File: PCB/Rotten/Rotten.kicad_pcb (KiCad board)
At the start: 2 copper layers, 56.5 x 61.6 mm, 43 parts, among them J1 Jack-DC, J2 FOOTSWITCH, J3 JACK OUTPUT, J4 JACK INPUT, Q1 2N5458, U1 AS301/OP07

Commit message: changed clipping diodes to 1N4148. Updated schematic and PCB images. Generated an HTML BOM.
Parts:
- D2, D3: value 1N4002 -> 1N4148
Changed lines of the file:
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@@
 		(tags "CP Radial series Radial pin pitch 2.00mm  diameter 5mm Electrolytic Capacitor")
 		(property "Reference" "C10"
-			(at 1 -3.75 360)
+			(at 1 -3.75 0)
 			(layer "F.SilkS")
 			(effects
@@
 		)
 		(property "Value" "4.7µF"
-			(at 1 3.75 360)
+			(at 1 3.75 0)
 			(layer "F.SilkS")
 			(effects
@@
 		)
 		(fp_text user "${REFERENCE}"
-			(at 1 0 360)
+			(at 1 0 0)
 			(layer "F.Fab")
 			(effects
@@
 		(tags "Resistor Axial_DIN0207 series Axial Horizontal pin pitch 7.62mm 0.25W = 1/4W length 6.3mm diameter 2.5mm")
 		(property "Reference" "R2"
-			(at 3.81 2.54 360)
+			(at 3.81 2.54 0)
 			(layer "F.SilkS")
 			(effects
@@
 		)
 		(property "Value" "100k"
-			(at 3.81 0 360)
+			(at 3.81 0 0)
 			(layer "F.SilkS")
 			(effects
@@
 		)
 		(fp_text user "${REFERENCE}"
-			(at 3.81 0 360)
+			(at 3.81 0 0)
 			(layer "F.Fab")
 			(effects
@@
 			)
 		)
-		(property "Value" "1N4002"
+		(property "Value" "1N4148"
 			(at 5.08 0 90)
 			(layer "F.SilkS")
@@
 		(tags "C Disc series Radial pin pitch 5.00mm  diameter 4.3mm width 1.9mm Capacitor")
 		(property "Reference" "C6"
-			(at -2.62 0 360)
+			(at -2.62 0 0)
 			(layer "F.SilkS")
 			(effects
@@
 		)
 		(property "Value" "100pF"
-			(at 2.5 0 360)
+			(at 2.5 0 0)
 			(layer "F.SilkS")
 			(effects
@@
 		)
 		(fp_text user "${REFERENCE}"
-			(at 2.5 0 360)
+			(at 2.5 0 0)
 			(layer "F.Fab")
 			(effects
@@
 		(tags "Resistor Axial_DIN0207 series Axial Horizontal pin pitch 7.62mm 0.25W = 1/4W length 6.3mm diameter 2.5mm")
 		(property "Reference" "R11"
-			(at 3.81 2.413 360)
+			(at 3.81 2.413 0)
 			(layer "F.SilkS")
 			(effects
@@
 		)
 		(property "Value" "1M"
-			(at 3.81 0 360)
+			(at 3.81 0 0)
 			(layer "F.SilkS")
 			(effects
@@
 		)
 		(fp_text user "${REFERENCE}"
-			(at 3.81 0 360)
+			(at 3.81 0 0)
 			(layer "F.Fab")
 			(effects
@@
 		(tags "C Disc series Radial pin pitch 5.00mm  diameter 4.3mm width 1.9mm Capacitor")
 		(property "Reference" "C7"
-			(at -2.58 0 360)
+			(at -2.58 0 0)
 			(layer "F.SilkS")
 			(effects
@@
 		)
 		(property "Value" "30pF"
-			(at 2.5 0 360)
+			(at 2.5 0 0)
 			(layer "F.SilkS")
 			(effects
@@
 		)
 		(fp_text user "${REFERENCE}"
-			(at 2.5 0 360)
+			(at 2.5 0 0)
 			(layer "F.Fab")
 			(effects
@@
 		)
 		(property "Value" "100k-A"
-			(at 2.54 2.54 360)
+			(at 2.54 2.54 0)
 			(layer "F.SilkS")
 			(effects
@@
 		)
 		(fp_text user "${REFERENCE}"
-			(at 0 2.54 360)
+			(at 0 2.54 0)
 			(layer "F.Fab")
 			(effects
@@
 		(tags "C Disc series Radial pin pitch 5.00mm  diameter 4.3mm width 1.9mm Capacitor")
 		(property "Reference" "C11"
-			(at 2.5 -2.2 360)
+			(at 2.5 -2.2 0)
 			(layer "F.SilkS")
 			(effects
@@
 		)
 		(property "Value" "3.3nF"
-			(at 2.5 0 360)
+			(at 2.5 0 0)
 			(layer "F.SilkS")
 			(effects
@@
 		)
 		(fp_text user "${REFERENCE}"
-			(at 2.5 0 360)
+			(at 2.5 0 0)
 			(layer "F.Fab")
 			(effects
@@
 		(tags "LED diameter 5.0mm 2 pins")
 		(property "Reference" "D4"
-			(at 1.27 -3.96 360)
+			(at 1.27 -3.96 0)
 			(layer "F.SilkS")
 			(effects
@@
 		)
 		(fp_text user "${REFERENCE}"
-			(at 1.25 0 360)
+			(at 1.25 0 0)
 			(layer "F.Fab")
 			(effects
@@
 		(tags "Through hole pin header THT 1x02 2.54mm single row")
 		(property "Reference" "J3"
-			(at 0 -2.33 360)
+			(at 0 -2.33 0)
 			(layer "F.SilkS")
 			(effects
@@
 		)
 		(property "Value" "JACK OUTPUT"
-			(at 0 4.87 360)
+			(at 0 4.87 0)
 			(layer "F.Fab")
 			(effects
@@
 		)
 		(property "Value" "Jack-DC"
-			(at 2.413 1.27 360)
+			(at 2.413 1.27 0)
 			(layer "F.SilkS")
 			(effects
@@
 		)
 		(fp_text user "${REFERENCE}"
-			(at 0 1.27 360)
+			(at 0 1.27 0)
 			(layer "F.Fab")
 			(effects
@@
 		)
 		(property "Value" "FOOTSWITCH"
-			(at -2.54 6.35 360)
+			(at -2.54 6.35 0)
 			(layer "F.SilkS")
 			(effects
@@
 		)
 		(fp_text user "${REFERENCE}"
-			(at 0 6.35 360)
+			(at 0 6.35 0)
 			(layer "F.Fab")
 			(effects
@@
 		)
 		(property "Value" "100k-A"
-			(at 2.54 2.54 360)
+			(at 2.54 2.54 0)
 			(layer "F.SilkS")
 			(effects
@@
 		)
 		(fp_text user "${REFERENCE}"
-			(at 0 2.54 360)
+			(at 0 2.54 0)
 			(layer "F.Fab")
 			(effects
@@
 		(tags "CP Radial series Radial pin pitch 2.00mm  diameter 5mm Electrolytic Capacitor")
 		(property "Reference" "C3"
-			(at 1 -3.75 360)
+			(at 1 -3.75 0)
 			(layer "F.SilkS")
 			(effects
@@
 		)
 		(property "Value" "1µF"
-			(at 1 3.75 360)
+			(at 1 3.75 0)
 			(layer "F.SilkS")
 			(effects
@@
 		)
 		(fp_text user "${REFERENCE}"
-			(at 1 0 360)
+			(at 1 0 0)
 			(layer "F.Fab")
 			(effects
@@
 		(tags "Resistor Axial_DIN0207 series Axial Horizontal pin pitch 7.62mm 0.25W = 1/4W length 6.3mm diameter 2.5mm")
 		(property "Reference" "R10"
-			(at 3.81 -2.37 360)
+			(at 3.81 -2.37 0)
 			(layer "F.SilkS")
 			(effects
@@
 		)
 		(property "Value" "1k5"
-			(at 3.81 0 360)
+			(at 3.81 0 0)
 			(layer "F.SilkS")
 			(effects
@@
 		)
 		(fp_text user "${REFERENCE}"
-			(at 3.81 0 360)
+			(at 3.81 0 0)
 			(layer "F.Fab")
 			(effects
@@
 			)
 		)
-		(property "Value" "1N4002"
+		(property "Value" "1N4148"
 			(at 5.08 0 90)
 			(layer "F.SilkS")
@@
 		(tags "C Disc series Radial pin pitch 5.00mm  diameter 4.3mm width 1.9mm Capacitor")
 		(property "Reference" "C12"
-			(at 2.46 2.159 360)
+			(at 2.46 2.159 0)
 			(layer "F.SilkS")
 			(effects
@@
 		)
 		(property "Value" "22nF"
-			(at 2.5 0 360)
+			(at 2.5 0 0)
 			(layer "F.SilkS")
 			(effects
@@
 		)
 		(fp_text user "${REFERENCE}"
-			(at 2.5 0 360)
+			(at 2.5 0 0)
 			(layer "F.Fab")
 			(effects
@@
 		)
 		(fp_text user "${REFERENCE}"
-			(at 0 2.54 360)
+			(at 0 2.54 0)
 			(layer "F.Fab")
 			(effects
@@
 	)
 	(zone
+		(net 18)
+		(net_name "Net-(D2-K)")
+		(layer "F.Cu")
+		(name "$teardrop_padvia$")
+		(hatch full 0.1)
+		(priority 30000)
+		(attr
+			(teardrop
+				(type padvia)
+			)
+		)
+		(connect_pads yes
+			(clearance 0)
+		)
+		(min_thickness 0.0254)
+		(filled_areas_thickness no)
+		(fill yes
+			(thermal_gap 0.5)
+			(thermal_bridge_width 0.5)
+			(island_removal_mode 1)
+			(island_area_min 10)
+		)
+		(polygon
+			(pts
+				(xy 138.14 65.967) (xy 138.14 66.367) (xy 139.794703 67.167) (xy 140.241 66.167) (xy 139.794703 65.167)
+			)
+		)
+	)
+	(zone
 		(net 6)
 		(net_name "Net-(C10-Pad1)")
@@
 		(name "$teardrop_padvia$")
 		(hatch full 0.1)
-		(priority 30003)
-		(attr
-			(teardrop
-				(type padvia)
-			)
-		)
-		(connect_pads yes
-			(clearance 0)
-		)
-		(min_thickness 0.0254)
-		(filled_areas_thickness no)
-		(fill yes
-			(thermal_gap 0.5)
-			(thermal_bridge_width 0.5)
-			(island_removal_mode 1)
-			(island_area_min 10)
-		)
-		(polygon
-			(pts
-				(xy 134.33 65.967) (xy 134.33 66.367) (xy 135.33 67.167) (xy 136.431 66.167) (xy 135.33 65.167)
-			)
-		)
-	)
-	(zone
-		(net 18)
-		(net_name "Net-(D2-K)")
-		(layer "F.Cu")
-		(name "$teardrop_padvia$")
-		(hatch full 0.1)
 		(priority 30010)
 		(attr
@@
 	)
 	(zone
+		(net 18)
+		(net_name "Net-(D2-K)")
+		(layer "F.Cu")
+		(name "$teardrop_padvia$")
+		(hatch full 0.1)
+		(priority 30002)
+		(attr
+			(teardrop
+				(type padvia)
+			)
+		)
+		(connect_pads yes
+			(clearance 0)
+		)
+		(min_thickness 0.0254)
+		(filled_areas_thickness no)
+		(fill yes
+			(thermal_gap 0.5)
+			(thermal_bridge_width 0.5)
+			(island_removal_mode 1)
+			(island_area_min 10)
+		)
+		(polygon
+			(pts
+				(xy 138.53 66.367) (xy 138.53 65.967) (xy 137.53 65.167) (xy 136.429 66.167) (xy 137.53 67.167)
+			)
+		)
+	)
+	(zone
 		(net 21)
 		(net_name "/VOUT")
@@
 	)
 	(zone
-		(net 18)
-		(net_name "Net-(D2-K)")
-		(layer "F.Cu")
-		(name "$teardrop_padvia$")
-		(hatch full 0.1)
-		(priority 30001)
-		(attr
-			(teardrop
-				(type padvia)
-			)
-		)
-		(connect_pads yes
-			(clearance 0)
-		)
-		(min_thickness 0.0254)
-		(filled_areas_thickness no)
-		(fill yes
-			(thermal_gap 0.5)
-			(thermal_bridge_width 0.5)
-			(island_removal_mode 1)
-			(island_area_min 10)
-		)
-		(polygon
-			(pts
-				(xy 138.14 65.967) (xy 138.14 66.367) (xy 139.794703 67.167) (xy 140.241 66.167) (xy 139.794703 65.167)
-			)
-		)
-	)
-	(zone
 		(net 6)
 		(net_name "Net-(C10-Pad1)")
@@
 		(name "$teardrop_padvia$")
 		(hatch full 0.1)
-		(priority 30002)
+		(priority 30001)
 		(attr
 			(teardrop
@@
 		(polygon
 			(pts
-				(xy 138.53 66.367) (xy 138.53 65.967) (xy 137.53 65.167) (xy 136.429 66.167) (xy 137.53 67.167)
+				(xy 134.33 65.967) (xy 134.33 66.367) (xy 135.33 67.167) (xy 136.431 66.167) (xy 135.33 65.167)
 			)
 		)

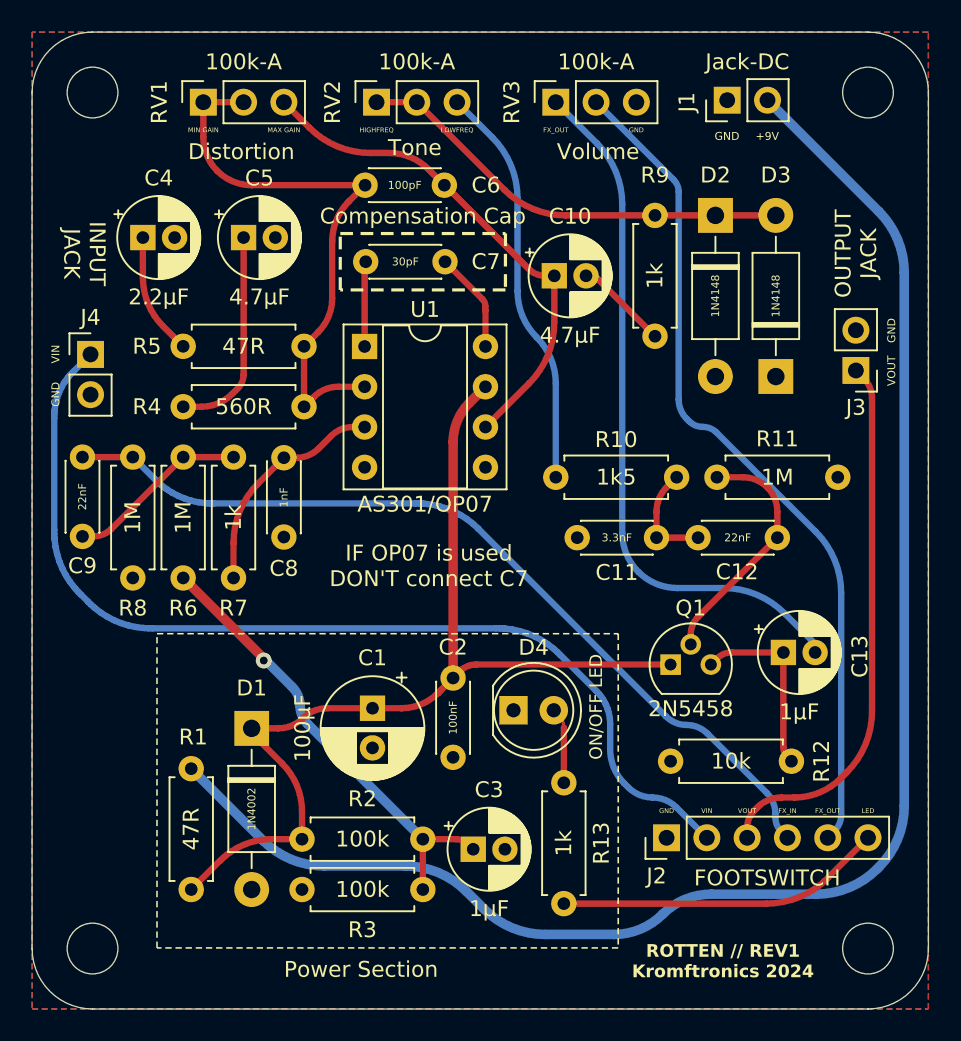
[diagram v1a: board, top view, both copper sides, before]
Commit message: Created Rev2 update! Fixed LED footswitch error that resulted in no light. Flipped "volume" and "gain" connections on PCB (1 -> 3). Fixed wrong pinout on JFET that resulted in no audio. Updated README with new images and better build descriptions.
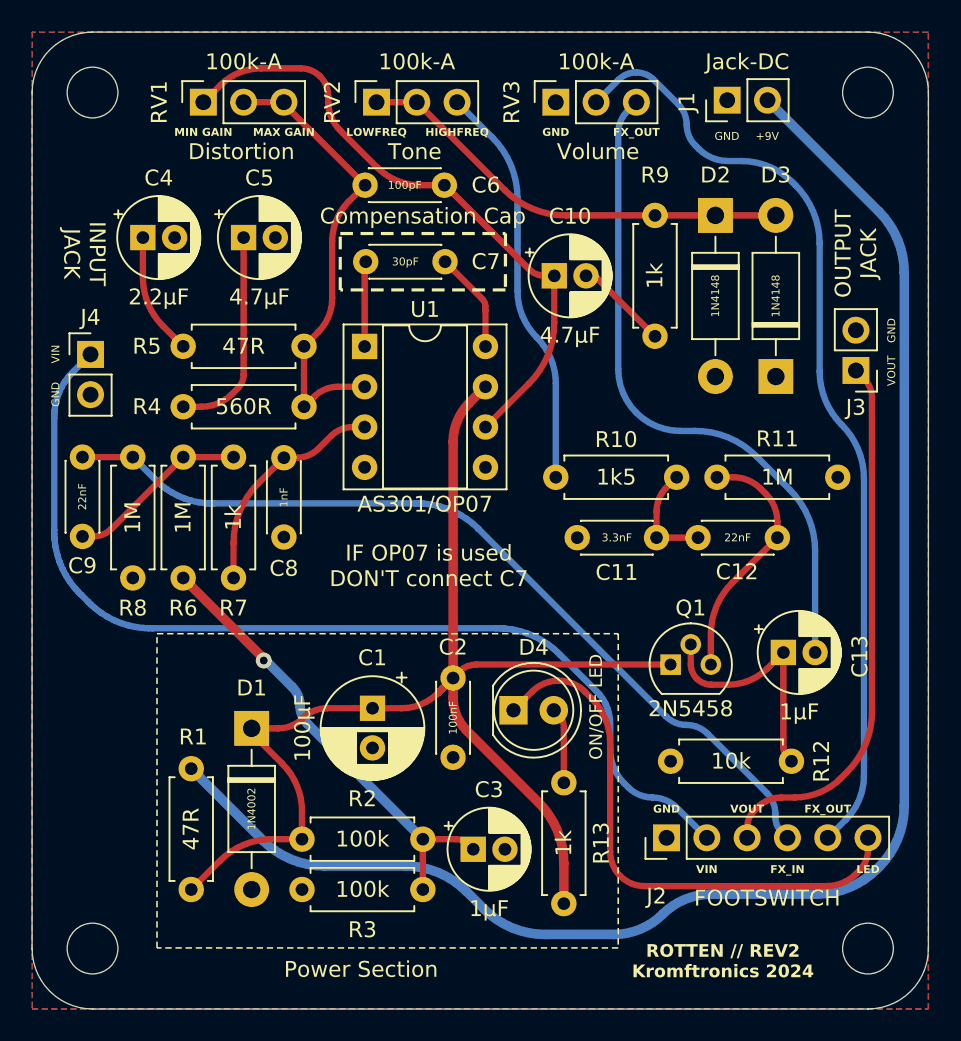
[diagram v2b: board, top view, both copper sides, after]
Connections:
- D4 pad 1: GND -> /LED
- Q1 pad 2: Net-(Q1-G) -> Net-(Q1-S)
- Q1 pad 3: Net-(Q1-S) -> Net-(Q1-G)
- R13 pad 2: /LED -> +9V
- RV1 pad 1: Net-(U1--) -> Net-(C10-Pad1)
- RV1 pad 3: Net-(C10-Pad1) -> Net-(U1--)
- RV3 pad 1: Net-(C13-Pad2) -> GND
- RV3 pad 3: GND -> Net-(C13-Pad2)
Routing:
- net +9V: track 62.8 -> 79.5 mm
- net /LED: track 20.6 -> 35.3 mm
- net Net-(C10-Pad1): track 31.9 -> 39.8 mm
- net Net-(U1--): track 35.6 -> 28.9 mm
- net /FX_OUT: track 53.1 -> 59.5 mm
- net Net-(Q1-S): track 11.9 -> 15.5 mm
- net Net-(C13-Pad2): track 44.4 -> 42.1 mm
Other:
- board text added: "ROTTEN // REV2 Kromftronics 2024"
- board text removed: "ROTTEN // REV1 Kromftronics 2024"

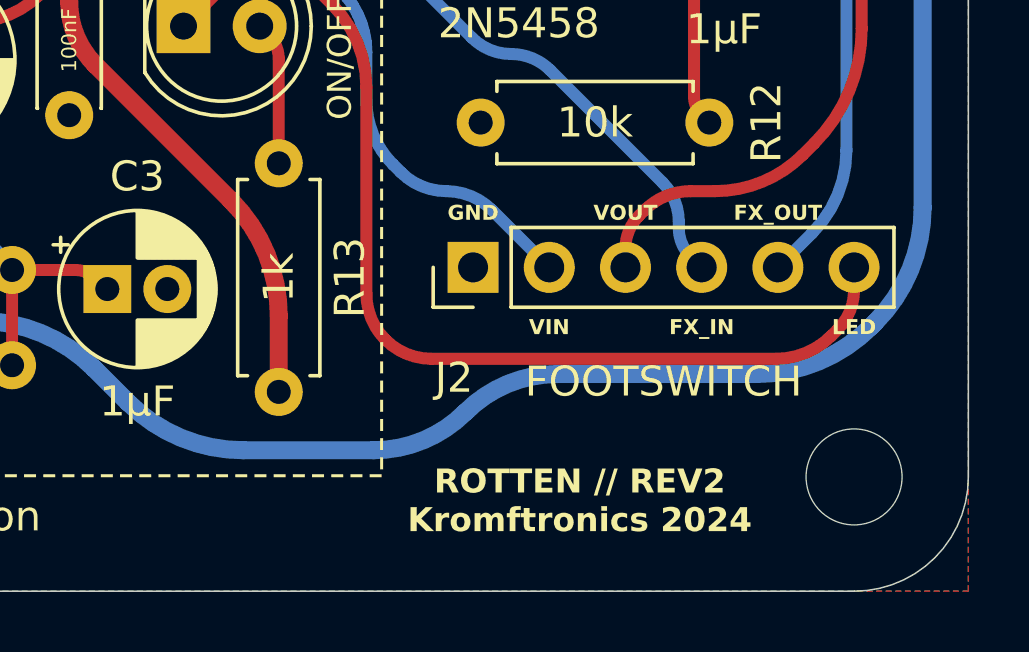
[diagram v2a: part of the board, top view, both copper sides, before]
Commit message: Added variable revision and issue date on the silkscreen, so I don't forget to update the rev and issue date on the silkscreen.
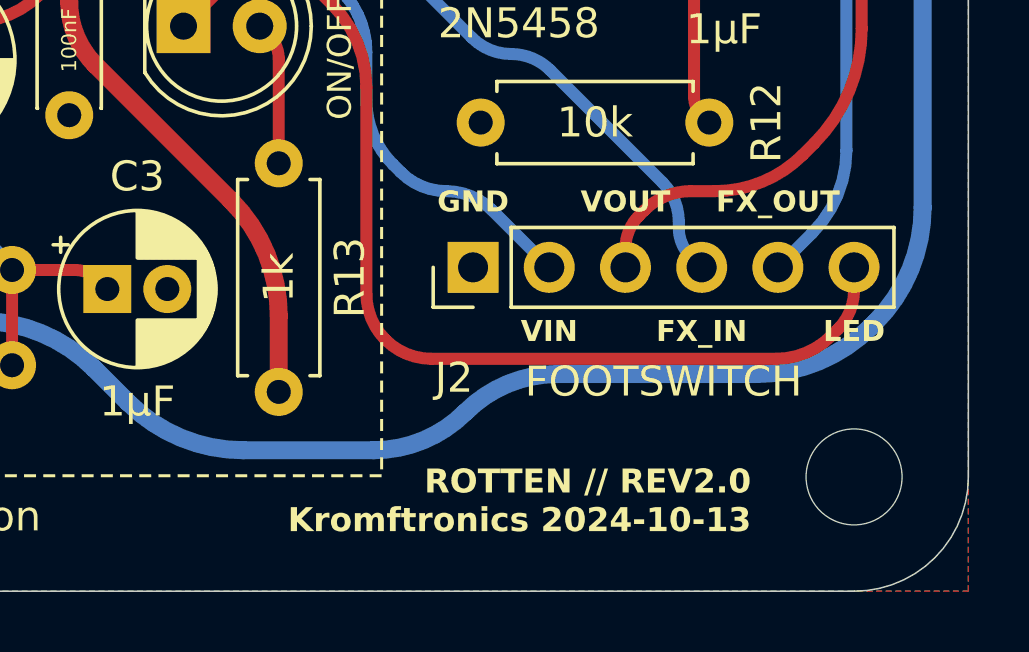
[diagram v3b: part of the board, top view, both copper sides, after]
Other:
- board text added: "ROTTEN // REV${REVISION} ${COMPANY} ${ISSUE_DATE}"
- board text removed: "ROTTEN // REV2 Kromftronics 2024"
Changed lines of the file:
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@@
 		(title "Rotten")
 		(date "2024-10-13")
-		(rev "2")
+		(rev "2.0")
 		(company "Kromftronics")
 	)
@@
 	)
 	(gr_text "VIN"
-		(at 135.89 107.696 0)
+		(at 135.89 107.95 0)
 		(layer "F.SilkS")
 		(effects
 			(font
-				(size 0.5 0.5)
+				(size 0.7 0.7)
 				(thickness 0.1)
 				(bold yes)
@@
 	)
 	(gr_text "GND"
-		(at 133.35 103.886 0)
+		(at 133.35 103.632 0)
 		(layer "F.SilkS")
 		(effects
 			(font
-				(size 0.5 0.5)
+				(size 0.7 0.7)
 				(thickness 0.1)
 				(bold yes)
@@
 	)
 	(gr_text "FX_IN"
-		(at 140.97 107.696 0)
+		(at 140.97 107.95 0)
 		(layer "F.SilkS")
 		(effects
 			(font
-				(size 0.5 0.5)
+				(size 0.7 0.7)
 				(thickness 0.1)
 				(bold yes)
@@
 	)
 	(gr_text "VOUT"
-		(at 138.43 103.886 0)
+		(at 138.43 103.632 0)
 		(layer "F.SilkS")
 		(effects
 			(font
-				(size 0.5 0.5)
+				(size 0.7 0.7)
 				(thickness 0.1)
 				(bold yes)
@@
 	)
 	(gr_text "LED"
-		(at 146.05 107.696 0)
+		(at 146.05 107.95 0)
 		(layer "F.SilkS")
 		(effects
 			(font
-				(size 0.5 0.5)
+				(size 0.7 0.7)
 				(thickness 0.1)
 				(bold yes)
@@
 		)
 	)
-	(gr_text "ROTTEN // REV2\nKromftronics 2024\n"
-		(at 136.906 114.3 0)
+	(gr_text "ROTTEN // REV${REVISION}\n${COMPANY} ${ISSUE_DATE}\n"
+		(at 142.621 114.3 0)
 		(layer "F.SilkS")
 		(effects
@@
 				(bold yes)
 			)
-			(justify bottom)
+			(justify right bottom)
 		)
 	)
@@
 	)
 	(gr_text "FX_OUT"
-		(at 143.51 103.886 0)
+		(at 143.51 103.632 0)
 		(layer "F.SilkS")
 		(effects
 			(font
-				(size 0.5 0.5)
+				(size 0.7 0.7)
 				(thickness 0.1)
 				(bold yes)
